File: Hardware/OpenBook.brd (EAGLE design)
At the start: 170.2 x 111.2 mm, 103 parts, among them IC1 BD5229G-TR, IC4 XC6220A331MR-G, J1 FH34SRJ-24S-0.5SH_99_, J2 SAMACSYS_PARTS_USB4110-GF-A, J3 QWIIC_RIGHT_ANGLE, J4 112A-TAAR-R03_ATTEND, Q1 20V/4.2A/52mΩ/1.4W, Q2 20V/4.2A/52mΩ/1.4W, Q3 SI1308EDL-T1-GE3, U0 ESP32_WROVER_SPARKFUN-IC-POWE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, U1 W25Q512JVEIQ, U2 ESP32-C6-WROOM-1-N8, U3 DS3231SN#, U4 MAX17048G+T10

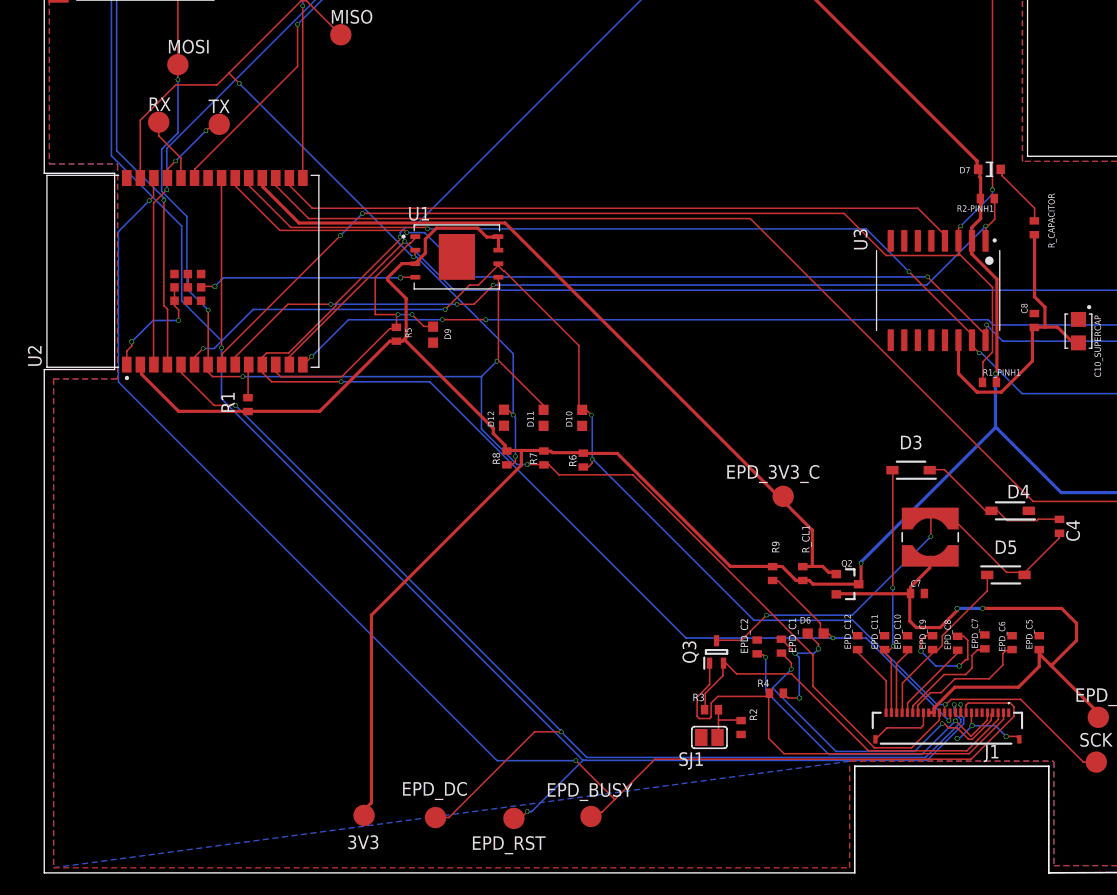
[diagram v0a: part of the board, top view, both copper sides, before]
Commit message: fixed pcb thickness and unfilled areas in GND plane
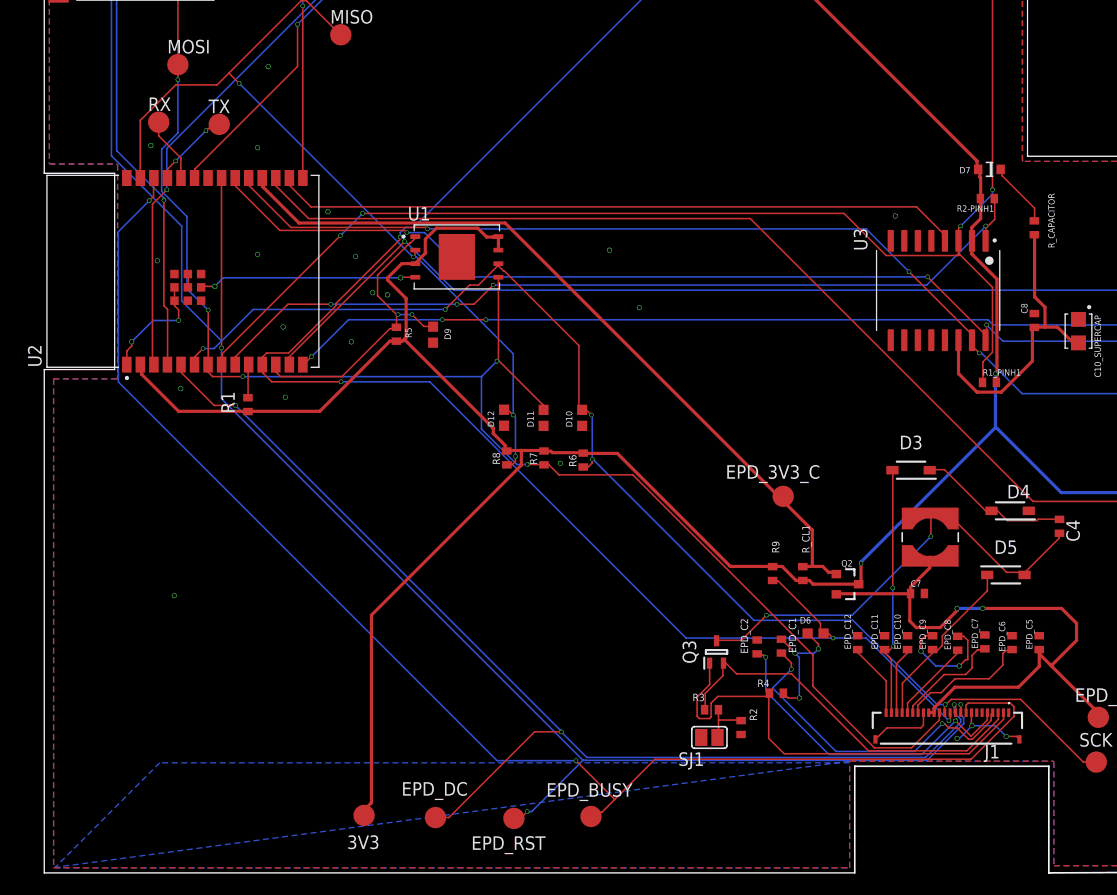
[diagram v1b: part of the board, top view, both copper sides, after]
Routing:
- net FLASH_CS: track 30.1 -> 28.7 mm
- net GND: vias 20 -> 38
